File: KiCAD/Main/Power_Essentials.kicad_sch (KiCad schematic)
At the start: 5 parts, among them J1 USB_C_Receptacle_USB2.0_16P, J2 USB_A, J3 USB_A, J4 Screw_Terminal_01x09, J5 Screw_Terminal_01x09

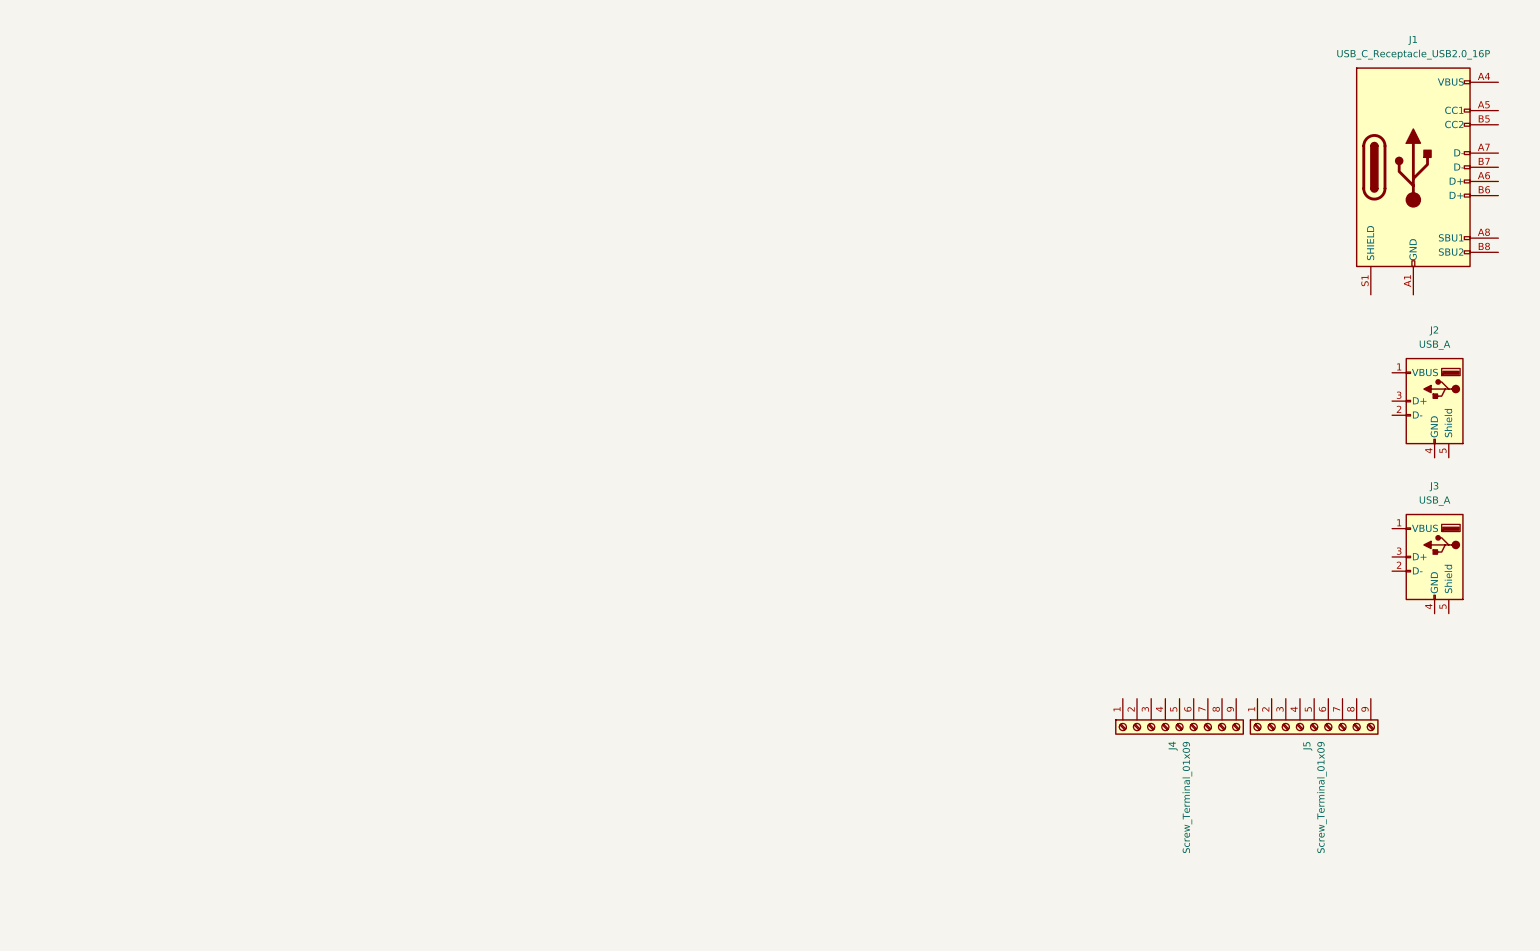
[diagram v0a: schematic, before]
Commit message: Update power modules
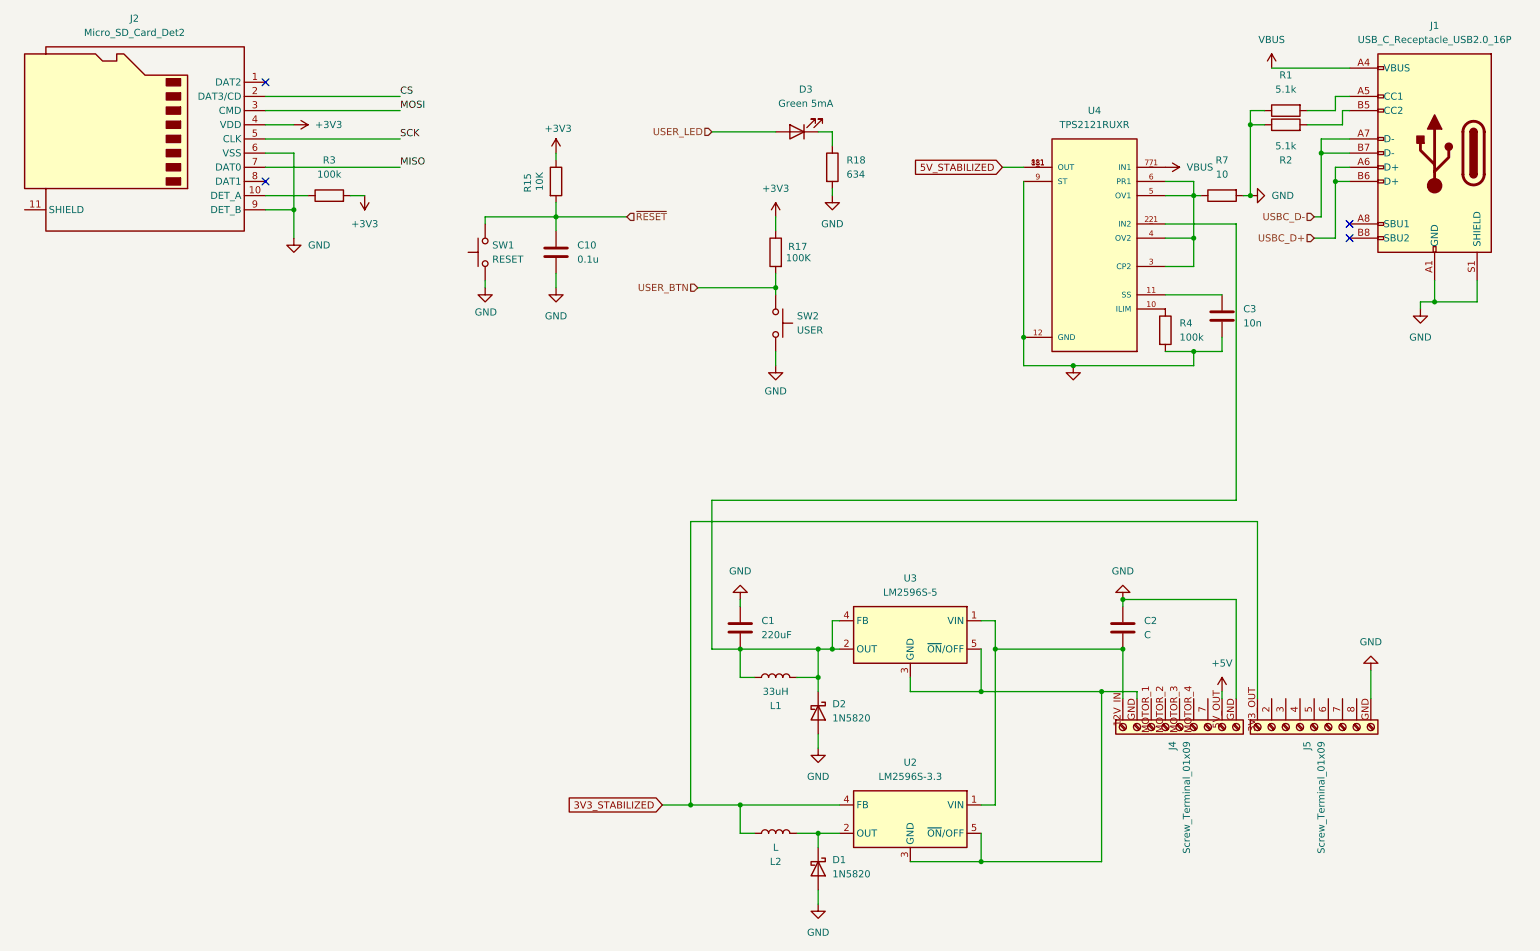
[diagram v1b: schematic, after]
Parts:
- removed J2, J3: USB_A, symbol Connector:USB_A
- added C1: 220uF, symbol Device:C
- added C10: 0.1u, Capacitor_SMD:C_0603_1608Metric, symbol Device:C
- added C2: C, symbol Device:C
- added C3: 10n, symbol Device:C
- added D1, D2: 1N5820, Diode_THT:D_DO-201AD_P15.24mm_Horizontal, symbol Diode:1N5820
- added D3: Green 5mA, LED_SMD:LED_0603_1608Metric, symbol Device:LED
- added J2: Micro_SD_Card_Det2, symbol Connector:Micro_SD_Card_Det2
- added L1: 33uH, symbol Device:L
- added L2: L, symbol Device:L
- added R1, R2: 5.1k, symbol Device:R
- added R15: 10K, Resistor_SMD:R_0603_1608Metric, symbol Device:R
- added R17: 100K, Resistor_SMD:R_0603_1608Metric, symbol Device:R
- added R18: 634, Resistor_SMD:R_0603_1608Metric, symbol Device:R
- added R3, R4: 100k, symbol Device:R
- added R7: 10, symbol Device:R
- added SW1: RESET, Button_Switch_SMD:SW_Push_1P1T_NO_Vertical_Wuerth_434133025816, symbol Switch:SW_Push
- added SW2: USER, Button_Switch_SMD:SW_Push_1P1T_NO_Vertical_Wuerth_434133025816, symbol Switch:SW_Push
- added U2: LM2596S-3.3, Package_TO_SOT_SMD:TO-263-5_TabPin3, symbol Regulator_Switching:LM2596S-3.3
- added U3: LM2596S-5, Package_TO_SOT_SMD:TO-263-5_TabPin3, symbol Regulator_Switching:LM2596S-5
- added U4: TPS2121RUXR, TPS2121RUXR:IC_TPS2121RUXR, symbol TPS2121RUXR:TPS2121RUXR
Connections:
- net GND: now reaches J1.A1 (GND), J1.A12 (GND), J1.B1 (GND), J1.B12 (GND)
- net GND: now also J1.S1 (SHIELD), J4.GND, J5.GND, C1.1, C10.2, C2.1, C3.2, D1.2 (A), D2.2 (A), J2.6 (VSS), J2.9 (DET_B), R1.1, R18.2, R2.1, R4.2, R7.2, SW1.1, SW2.1, U4.12 (GND), U4.9 (ST)
- net VBUS: now reaches J1.A4 (VBUS), J1.A9 (VBUS), J1.B4 (VBUS), J1.B9 (VBUS)
- net VBUS: now also U4.7 (IN1), U4.7_1 (IN1)
- net at J1.A5 (CC1): now also R1.2
- net USBC_D+: now reaches J1.A6 (D+)
- net USBC_D+: now also J1.B6 (D+)
- net USBC_D-: now reaches J1.A7 (D-)
- net USBC_D-: now also J1.B7 (D-)
- net at J1.B5 (CC2): now also R2.2
- new net: D3.1 (K), R18.1
- new net: R4.1, U4.10 (ILIM)
- new net: C3.1, U4.11 (SS)
- new net: C1.2, D2.1 (K), L1.1, L1.2, U3.2 (OUT), U3.4 (FB), U4.2 (IN2), U4.2_1 (IN2)
- new net: R7.1, U4.3 (CP2), U4.4 (OV2), U4.5 (OV1), U4.6 (PR1)
- new net: D1.1 (K), L2.2, U2.2 (OUT)
- new net: C2.2, J4.12V_IN, U2.1 (VIN), U3.1 (VIN)
- new net: J4.GND, U2.3 (GND), U2.5 (~{ON}/OFF), U3.3 (GND), U3.5 (~{ON}/OFF)
- new net: J2.10 (DET_A), R3.1
- new net +3V3: J2.4 (VDD), R15.1, R17.1, R3.2
- new net +5V: J4.5V_OUT
- new net 3V3_STABILIZED: J5.3V3_OUT, L2.1, U2.4 (FB)
- new net 5V_STABILIZED: U4.1 (OUT), U4.1_1 (OUT), U4.8 (OUT), U4.8_1 (OUT)
- new net CS: J2.2 (DAT3/CD)
- new net MISO: J2.7 (DAT0)
- new net MOSI: J2.3 (CMD)
- new net SCK: J2.5 (CLK)
- new net USER_BTN: R17.2, SW2.2
- new net USER_LED: D3.2 (A)
- new net ~{RESET}: C10.1, R15.2, SW1.2
- no-connect marks 0 -> 4
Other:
- moved on the sheet: J1, J4, J5

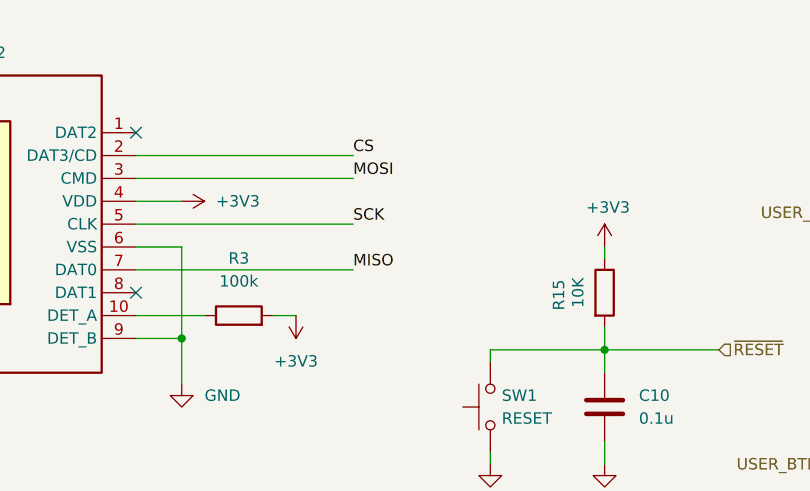
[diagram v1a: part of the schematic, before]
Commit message: Update MCU to display connections
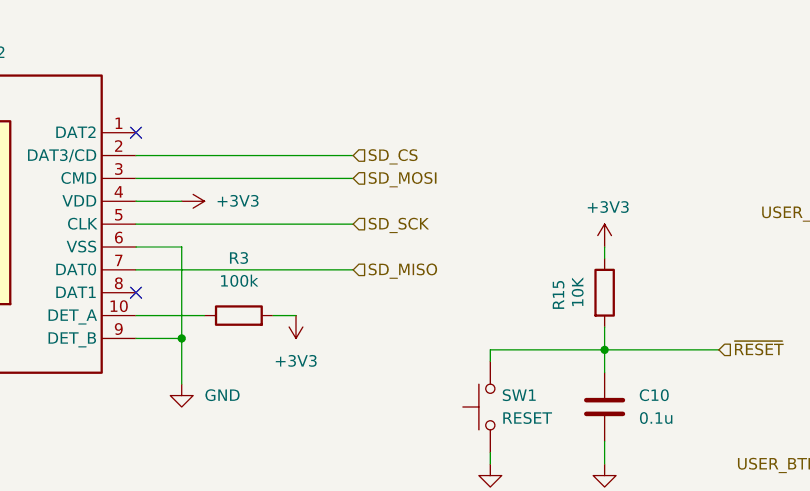
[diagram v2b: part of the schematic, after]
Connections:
- net CS renamed SD_CS
- net MISO renamed SD_MISO
- net MOSI renamed SD_MOSI
- net SCK renamed SD_SCK
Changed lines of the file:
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@@
-		)
-	)
-	(label "MOSI"
-		(at 83.82 29.21 0)
-		(effects
-			(font
-				(size 1.27 1.27)
-			)
-			(justify left bottom)
-		)
-	)
-	(label "MISO"
-		(at 83.82 39.37 0)
-		(effects
-			(font
-				(size 1.27 1.27)
-			)
-			(justify left bottom)
-		)
-	)
-	(label "CS"
-		(at 83.82 26.67 0)
-		(effects
-			(font
-				(size 1.27 1.27)
-			)
-			(justify left bottom)
-		)
-	)
-	(label "SCK"
-		(at 83.82 34.29 0)
-		(effects
-			(font
-				(size 1.27 1.27)
-			)
-			(justify left bottom)
 		)
 	)
@@
 		)
 	)
+	(hierarchical_label "SD_CS"
+		(shape input)
+		(at 83.82 26.67 0)
+		(effects
+			(font
+				(size 1.27 1.27)
+			)
+			(justify left)
+		)
+	)
 	(hierarchical_label "USBC_D+"
 		(shape input)
@@
 		)
 	)
+	(hierarchical_label "SD_SCK"
+		(shape input)
+		(at 83.82 34.29 0)
+		(effects
+			(font
+				(size 1.27 1.27)
+			)
+			(justify left)
+		)
+	)
+	(hierarchical_label "SD_MOSI"
+		(shape input)
+		(at 83.82 29.21 0)
+		(effects
+			(font
+				(size 1.27 1.27)
+			)
+			(justify left)
+		)
+	)
+	(hierarchical_label "SD_MISO"
+		(shape input)
+		(at 83.82 39.37 0)
+		(effects
+			(font
+				(size 1.27 1.27)
+			)
+			(justify left)
+		)
+	)

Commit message: Continue integrating
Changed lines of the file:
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@@
 		)
 	)
-	(global_label "3V3_STABILIZED"
+	(hierarchical_label "5V_STABILIZED"
 		(shape input)
-		(at 130.81 153.67 180)
-		(fields_autoplaced yes)
+		(at 191.77 39.37 180)
 		(effects
 			(font
@@
 			)
 			(justify right)
-		)
-		(property "Intersheetrefs" "${INTERSHEET_REFS}"
-			(at 112.9477 153.67 0)
-			(effects
-				(font
-					(size 1.27 1.27)
-				)
-				(justify right)
-				(hide yes)
-			)
-		)
-	)
-	(global_label "5V_STABILIZED"
-		(shape input)
-		(at 191.77 39.37 180)
-		(fields_autoplaced yes)
-		(effects
-			(font
-				(size 1.27 1.27)
-			)
-			(justify right)
-		)
-		(property "Intersheetrefs" "${INTERSHEET_REFS}"
-			(at 175.1172 39.37 0)
-			(effects
-				(font
-					(size 1.27 1.27)
-				)
-				(justify right)
-				(hide yes)
-			)
 		)
 	)
@@
 		)
 	)
+	(hierarchical_label "3V3_STABILIZED"
+		(shape input)
+		(at 130.81 153.67 180)
+		(effects
+			(font
+				(size 1.27 1.27)
+			)
+			(justify right)
+		)
+	)

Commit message: prep for merge
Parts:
- added Q1, Q2, Q3: BC108, Package_TO_SOT_THT:TO-18-3, symbol Transistor_BJT:BC108
- C1: value 220uF -> 220u
- C2: value C -> 680u
- L1: value 33uH -> 33u
- L2: value L -> 33u
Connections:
- net GND: now also Q1.1 (E), Q2.1 (E), Q3.1 (E)
- net at C2.2, U2.1 (VIN), U3.1 (VIN): now also J4.7.4V_IN, J4.7.4V_OUT; no longer J4.12V_IN
- net at J5.4 (Pin_4): now also Q1.3 (C)
- net at J5.5 (Pin_5): now also Q2.3 (C)
- net at J5.6 (Pin_6): now also Q3.3 (C)
- new net Drogue Backup Pyro: Q2.2 (B)
- new net Drogue Main Pyro: Q1.2 (B)
- new net Main Parachute Pyro: Q3.2 (B)

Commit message: Keep up to date
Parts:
- added D4, D5, D6: 1N5820, Diode_THT:D_DO-201AD_P15.24mm_Horizontal, symbol Diode:1N5820
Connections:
- net GND: now also U2.3 (GND), U2.5 (~{ON}/OFF), U3.3 (GND), U3.5 (~{ON}/OFF)
- net at Q3.3 (C): now also J5.Main_Parachute; no longer J5.6 (Pin_6)
- net at C2.2, J4.7.4V_IN, U2.1 (VIN)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: now also D4.2 (A), D5.2 (A), D6.2 (A); no longer J4.7.4V_OUT
- net at Q2.3 (C): now also J5.Drogue_Backup; no longer J5.5 (Pin_5)
- net at Q1.3 (C): now also J5.Drogue_Main; no longer J5.4 (Pin_4)
- new net: D4.1 (K), J5.Pyro_OUT_1
- new net: D6.1 (K), J5.Pyro_OUT_3
- new net: D5.1 (K), J5.Pyro_OUT_2
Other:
- moved on the sheet: C1, C10, C2, D1, D2, D3, J4, J5, L1, L2, Q1, Q2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

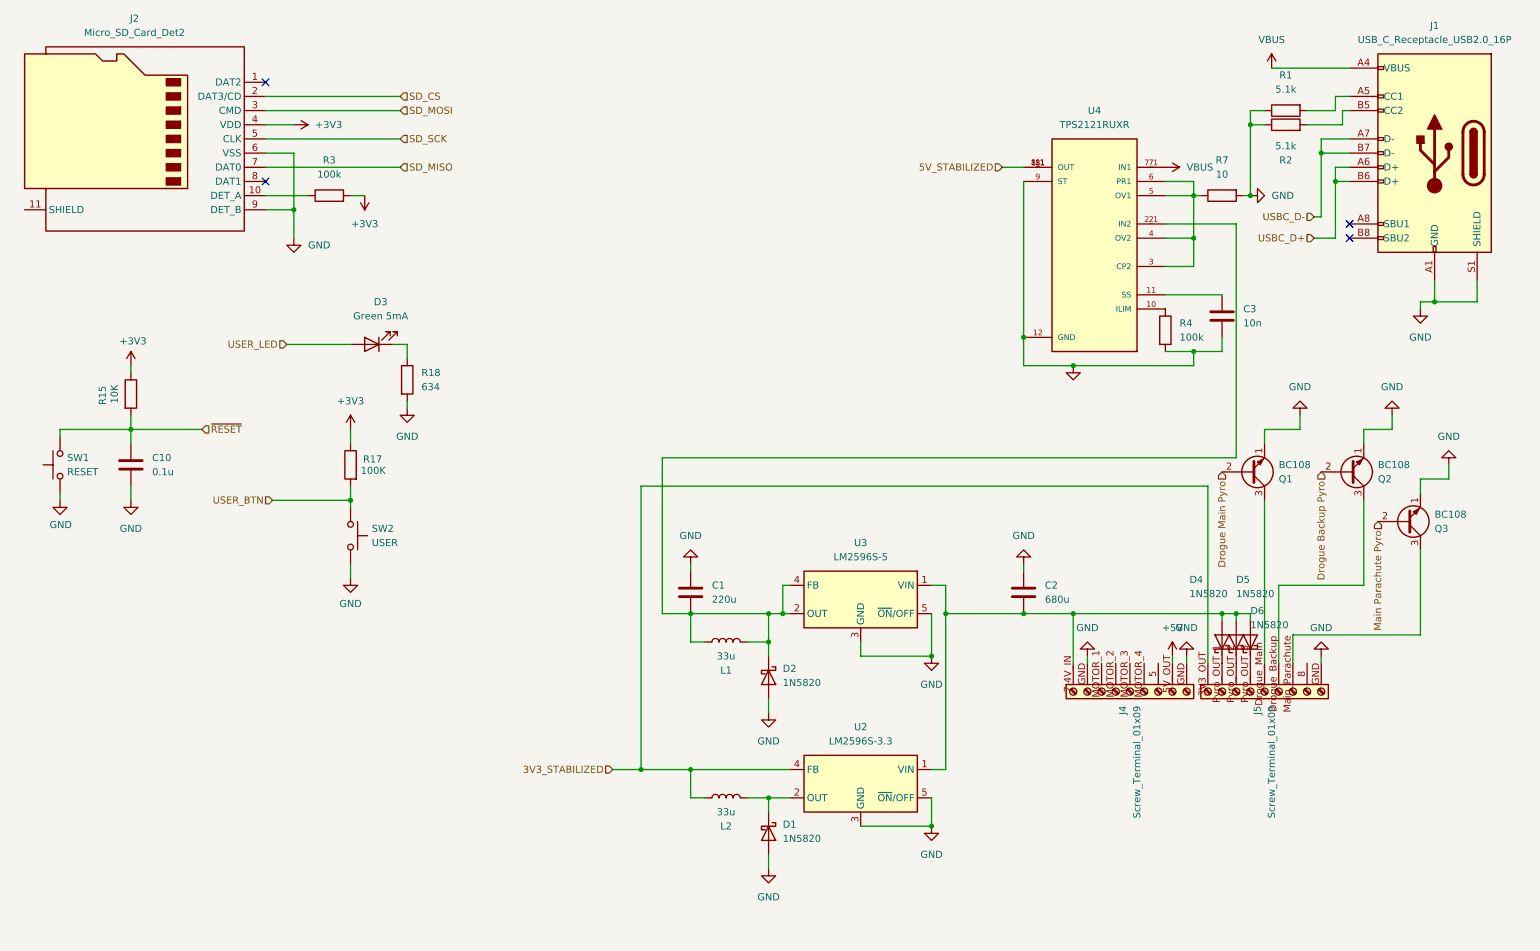
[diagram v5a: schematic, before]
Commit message: Create wiring diagram draft
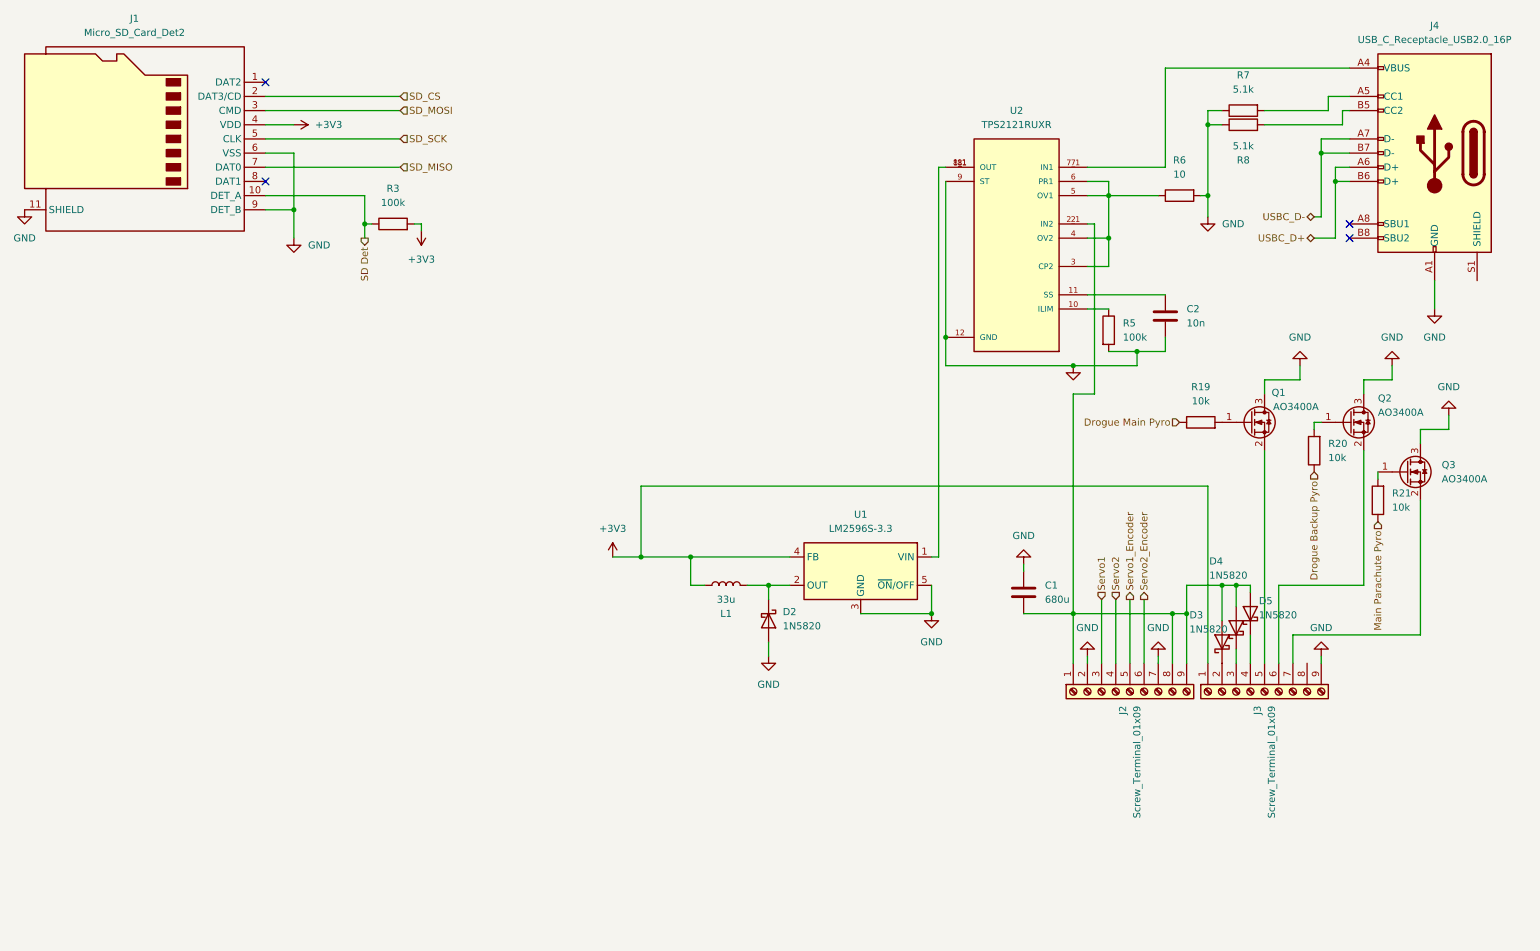
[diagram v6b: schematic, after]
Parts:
- removed C1: 220u, symbol Device:C
- removed C10: 0.1u, Capacitor_SMD:C_0603_1608Metric, symbol Device:C
- removed D2: 1N5820, Diode_THT:D_DO-201AD_P15.24mm_Horizontal, symbol Diode:1N5820
- removed D3: Green 5mA, LED_SMD:LED_0603_1608Metric, symbol Device:LED
- removed L1: 33u, symbol Device:L
- removed Q1, Q2, Q3: BC108, Package_TO_SOT_THT:TO-18-3, symbol Transistor_BJT:BC108
- removed R15: 10K, Resistor_SMD:R_0603_1608Metric, symbol Device:R
- removed R17: 100K, Resistor_SMD:R_0603_1608Metric, symbol Device:R
- removed R18: 634, Resistor_SMD:R_0603_1608Metric, symbol Device:R
- removed SW1: RESET, Button_Switch_SMD:SW_Push_1P1T_NO_Vertical_Wuerth_434133025816, symbol Switch:SW_Push
- removed SW2: USER, Button_Switch_SMD:SW_Push_1P1T_NO_Vertical_Wuerth_434133025816, symbol Switch:SW_Push
- removed U3: LM2596S-5, Package_TO_SOT_SMD:TO-263-5_TabPin3, symbol Regulator_Switching:LM2596S-5
- added Q1, Q2, Q3: AO3400A, Package_TO_SOT_SMD:SOT-23, symbol Transistor_FET:AO3400A
- added R19, R20, R21: 10k, symbol Device:R
- renumbered C2 to C1, C3 to C2, D1 to D2, D4 to D3, D5 to D4, D6 to D5, J2 to J1, J4 to J2, J5 to J3, J1 to J4, L2 to L1, R4 to R5, R7 to R6, R1 to R7, R2 to R8, U2 to U1, U4 to U2
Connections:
- net +3V3: now also J3.1 (3V3_OUT), L1.1, U1.4 (FB)
- net Drogue Backup Pyro: now also R20.1
- net Drogue Main Pyro: now also R19.1
- net GND: now also J1.11 (SHIELD), J2.2 (GND), J2.7 (MotorGND), J3.9 (GND), Q1.3 (D), Q2.3 (D), Q3.3 (D); no longer J2.GND, J3.GND, J4.S1 (SHIELD)
- net Main Parachute Pyro: now also R21.1
- net at U2.2 (IN2), U2.2_1 (IN2): now also C1.2, D3.2 (A), D4.2 (A), D5.2 (A), J2.1 (7.4V_IN), J2.8 (MotorPwr1), J2.9 (MotorPwr2)
- net at D3.1 (K): now also J3.2 (Pyro_OUT_1); no longer J3.Pyro_OUT_1
- net at D5.1 (K): now also J3.4 (Pyro_OUT_3); no longer J3.Pyro_OUT_3
- net SD Det: now reaches J1.10 (DET_A), R3.1
- net at D4.1 (K): now also J3.3 (Pyro_OUT_2); no longer J3.Pyro_OUT_2
- net Servo1_Encoder: now reaches J2.5 (Servo1_Encoder)
- removed net +5V: J2.5V_OUT
- removed net 3V3_STABILIZED: J3.3V3_OUT, L1.1, U1.4 (FB)
- net 5V_STABILIZED: no longer names the net of U2.1 (OUT), U2.1_1 (OUT), U2.8 (OUT), U2.8_1 (OUT)
- net 5V_STABILIZED: now also U1.1 (VIN)
- net VBUS: no longer names the net of J4.A4 (VBUS), J4.A9 (VBUS), J4.B4 (VBUS), J4.B9 (VBUS), U2.7 (IN1), U2.7_1 (IN1)
- new net: Q1.1 (G), R19.2
- new net: Q3.1 (G), R21.2
- new net: J3.7 (Main_Parachute), Q3.2 (S)
- new net: Q2.1 (G), R20.2
- new net: J3.6 (Drogue_Backup), Q2.2 (S)
- new net: J3.5 (Drogue_Main), Q1.2 (S)
- new net Servo1: J2.3 (Servo1)
- new net Servo2: J2.4 (Servo2)
- new net Servo2_Encoder: J2.6 (Servo2_Encoder)
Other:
- moved on the sheet: C2, D2, D4, D5, J2, J3, L1, R3, R5, R6, R7, R8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
